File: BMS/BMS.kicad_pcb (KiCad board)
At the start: 2 copper layers, 69.4 x 66 mm, 85 parts, among them J1 Cell Taps, J10 IsoSPI, J2 IsoSPI, J3 Temp Sensors, Q1 NSV1C201MZ4, Q2 BSS308PE, Q3 BSS308PE, Q4 BSS308PE, Q5 BSS308PE, Q6 BSS308PE, Q7 BSS308PE, Q8 BSS308PE, SW1 SW_DIP_x04, U1 LTC6811, U2 ADG708

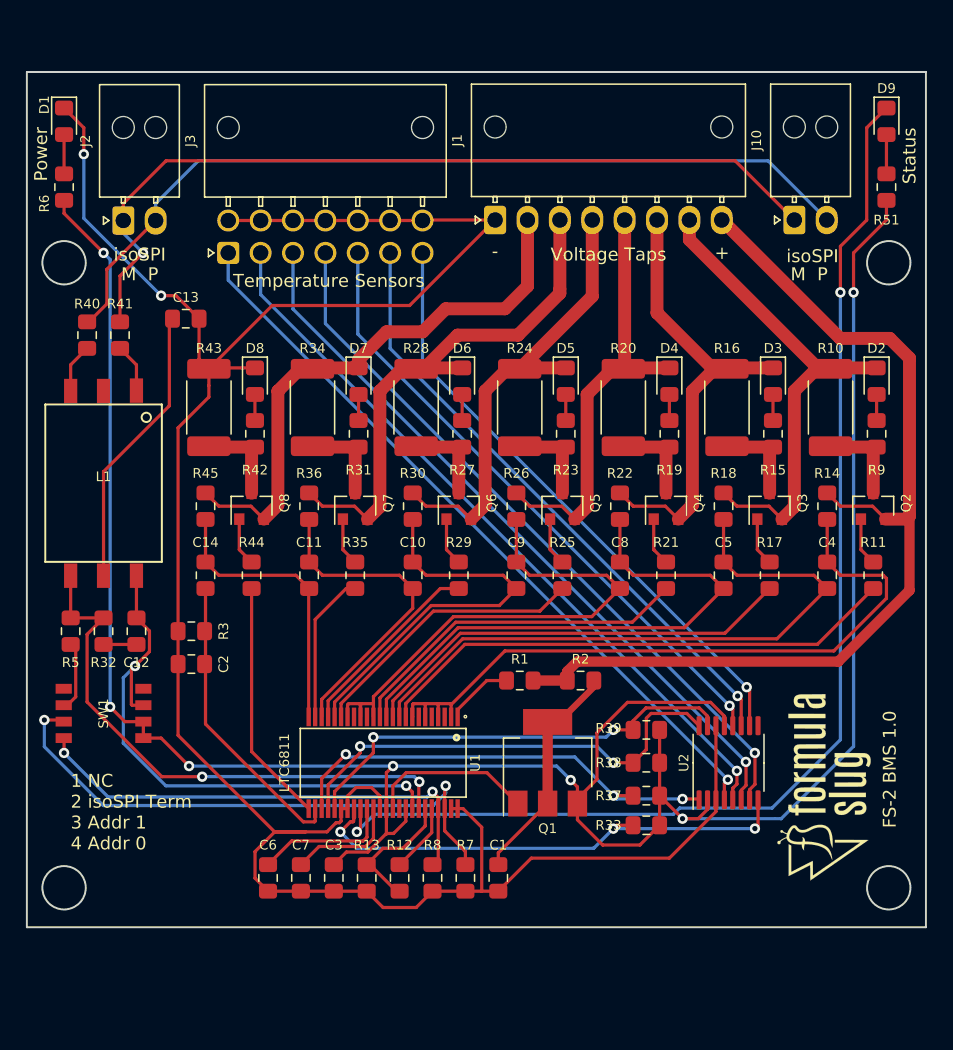
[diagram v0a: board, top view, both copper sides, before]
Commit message: Add PTC fusing to BMS board and finish layout v1.0
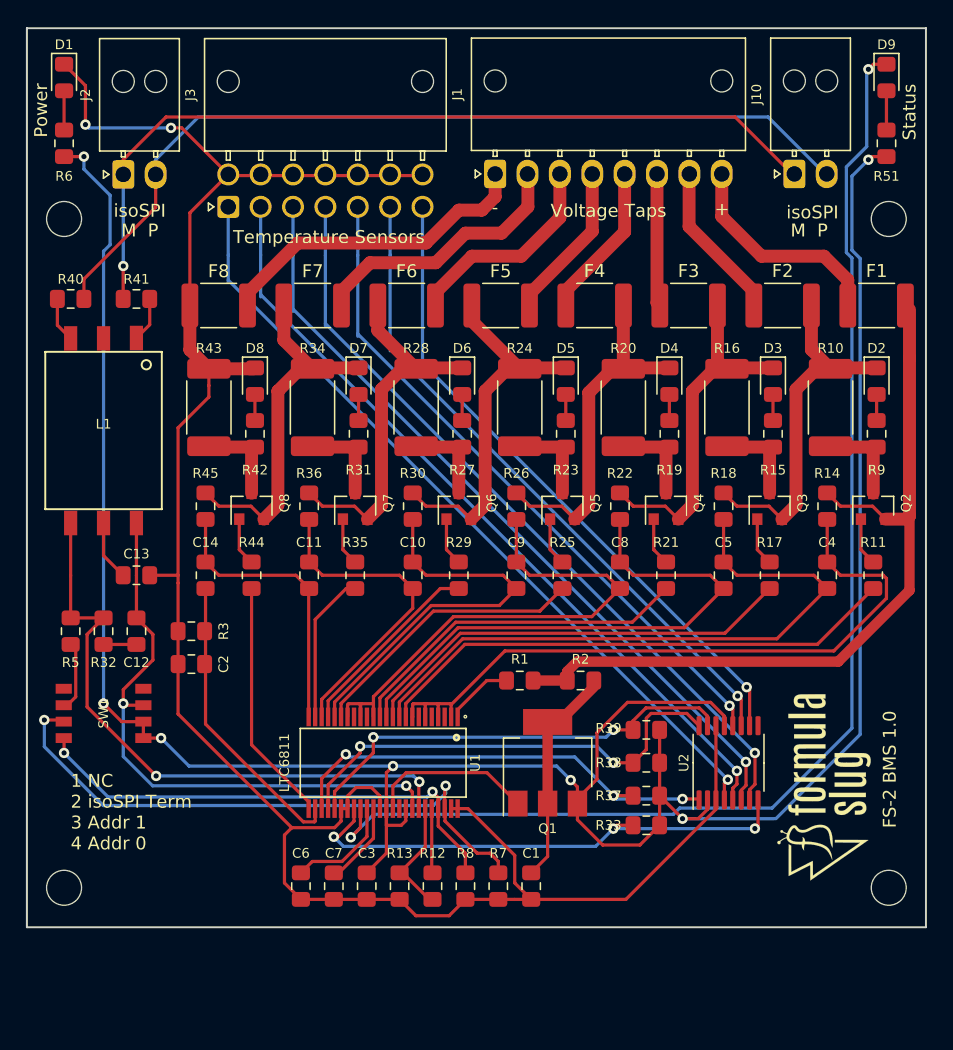
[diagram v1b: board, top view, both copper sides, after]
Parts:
- added ?: MountingHole_2.7mm_M2.5, MountingHole:MountingHole_2.7mm_M2.5, F.Cu at (90.9, 69.8)
- added ?: MountingHole_2.7mm_M2.5, MountingHole:MountingHole_2.7mm_M2.5, F.Cu at (90.9, 121.4)
- added ?: MountingHole_2.7mm_M2.5, MountingHole:MountingHole_2.7mm_M2.5, F.Cu at (154.6, 121.4)
- added ?: MountingHole_2.7mm_M2.5, MountingHole:MountingHole_2.7mm_M2.5, F.Cu at (154.7, 69.8)
- added F1: Polyfuse, Fuse:Fuse_1812_4532Metric_Pad1.30x3.40mm_HandSolder, F.Cu at (153.7, 76.5)
- added F2: Polyfuse, Fuse:Fuse_1812_4532Metric_Pad1.30x3.40mm_HandSolder, F.Cu at (146.4, 76.5)
- added F3: Polyfuse, Fuse:Fuse_1812_4532Metric_Pad1.30x3.40mm_HandSolder, F.Cu at (139.2, 76.5)
- added F4: Polyfuse, Fuse:Fuse_1812_4532Metric_Pad1.30x3.40mm_HandSolder, F.Cu at (131.9, 76.5)
- added F5: Polyfuse, Fuse:Fuse_1812_4532Metric_Pad1.30x3.40mm_HandSolder, F.Cu at (124.6, 76.5)
- added F6: Polyfuse, Fuse:Fuse_1812_4532Metric_Pad1.30x3.40mm_HandSolder, F.Cu at (117.4, 76.5)
- added F7: Polyfuse, Fuse:Fuse_1812_4532Metric_Pad1.30x3.40mm_HandSolder, F.Cu at (110.1, 76.5)
- added F8: Polyfuse, Fuse:Fuse_1812_4532Metric_Pad1.30x3.40mm_HandSolder, F.Cu at (102.9, 76.5)
- D1: value LTST-S220KGKT -> LH R974-LP-1
- moved C13 20.2 mm to (96.5, 97.3)
- moved L1 4.06 mm to (94.0, 86.1)
- moved J1 3.56 mm to (124.2, 66.3)
- moved J10 3.56 mm to (147.3, 66.3)
- moved J2 3.56 mm to (95.5, 66.3)
- moved J3 3.56 mm to (103.6, 68.8)
- moved R51 3.38 mm to (154.4, 63.9)
- moved R6 3.38 mm to (90.9, 63.9)
- moved D1 3.38 mm to (90.9, 58.9)
- moved D9 3.38 mm to (154.4, 58.9)
- moved R40 3.07 mm to (91.4, 75.9), turned to 180 degrees
- moved R41 3.07 mm to (96.5, 75.9), turned to 0 degrees
- moved C1 2.62 mm to (127.0, 121.3)
- moved C7 2.62 mm to (111.8, 121.3)
- moved R13 2.62 mm to (116.8, 121.3)
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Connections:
- J1 pad 1: V- -> Net-(F8-Pad2)
- J1 pad 2: /BB1/B# -> Net-(F7-Pad2)
- J1 pad 3: /BB2/B# -> Net-(F6-Pad2)
- J1 pad 4: /BB3/B# -> Net-(F5-Pad2)
- J1 pad 5: /BB4/B# -> Net-(F4-Pad2)
- J1 pad 6: /BB5/B# -> Net-(F3-Pad2)
- J1 pad 7: /BB6/B# -> Net-(F2-Pad2)
- J1 pad 8: /BB6/B#+1 -> Net-(F1-Pad2)
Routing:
- net Net-(F8-Pad2): track 0.00 -> 24.9 mm
- net V-: track 189.7 -> 166.9 mm
- net Net-(F7-Pad2): track 0.00 -> 21.0 mm
- net Net-(C13-Pad1): track 22.1 -> 4.66 mm
- net Net-(F1-Pad2): track 0.00 -> 17.0 mm
- net Net-(F6-Pad2): track 0.00 -> 16.4 mm
- net /BB1/B#: track 44.7 -> 29.4 mm
- net /BB6/B#+1: track 76.0 -> 61.3 mm
- net /BB2/B#: track 43.5 -> 30.4 mm
- net Net-(F2-Pad2): track 0.00 -> 12.2 mm
- net Net-(F5-Pad2): track 0.00 -> 12.2 mm
- net Net-(F4-Pad2): track 0.00 -> 12.0 mm
- net Net-(F3-Pad2): track 0.00 -> 10.2 mm
- net /BB6/B#: track 41.1 -> 30.9 mm
- net VREG: track 194.2 -> 202.9 mm
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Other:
- board size 69.4 x 66 mm -> 69.4 x 69.4 mm

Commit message: Layout v1.1 of BMS
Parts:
- removed the ? at (90.9, 69.8)
- removed the ? at (90.9, 121.4)
- removed the ? at (154.6, 121.4)
- removed the ? at (154.7, 69.8)
- removed the J3 at (103.6, 68.8)
- added ?: MountingHole_3.2mm_M3, MountingHole:MountingHole_3.2mm_M3, F.Cu at (101.9, 114.9)
- added ?: MountingHole_3.2mm_M3, MountingHole:MountingHole_3.2mm_M3, F.Cu at (101.9, 58.8)
- added ?: MountingHole_3.2mm_M3, MountingHole:MountingHole_3.2mm_M3, F.Cu at (153.7, 58.8)
- added ?: MountingHole_3.2mm_M3, MountingHole:MountingHole_3.2mm_M3, F.Cu at (153.7, 114.9)
- added J2: Temp Sensors, Connector_Molex:Molex_Nano-Fit_105314-xx14_2x07_P2.50mm_Horizontal, F.Cu at (108.8, 68.8)
- moved D9 78.0 mm to (118.0, 127.8)
- moved D1 76.8 mm to (124.8, 127.8)
- moved R51 72.4 mm to (120.3, 127.8), turned to 90 degrees
- moved R6 71.2 mm to (122.6, 127.8), turned to 90 degrees
- moved R40 70.6 mm to (145.9, 120.8), turned to 90 degrees
- moved R41 70.0 mm to (145.9, 125.5), turned to 270 degrees
- moved L1 56.1 mm to (136.1, 123.1), turned to 90 degrees
- moved J3 54.6 mm to (103.4, 120.4), turned to 270 degrees
- moved J4 54.6 mm to (154.7, 120.4), turned to 270 degrees
- moved R32 52.0 mm to (138.0, 129.3), turned to 180 degrees
- moved C12 46.4 mm to (133.7, 129.3), turned to 0 degrees
- moved C13 45.9 mm to (129.4, 129.3), turned to 180 degrees
- moved R5 38.1 mm to (123.3, 122.4), turned to 180 degrees
- moved R33 35.6 mm to (100.8, 110.1), turned to 180 degrees
- moved R37 35.6 mm to (100.8, 107.8), turned to 180 degrees
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- renumbered J2 to J3, J10 to J4
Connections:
- net /IsoSPI_N renamed /extIsoSPI_N
- net /IsoSPI_P renamed /extIsoSPI_P
- C12 pad 1: IMA -> IsoSPI_N
- L1 pad 4: IPA -> IsoSPI_P
- L1 pad 6: IMA -> IsoSPI_N
- R32 pad 1: IPA -> IsoSPI_P
- R5 pad 1: Net-(R5-Pad1) -> IsoSPI_N
- R5 pad 2: IPA -> Net-(R5-Pad2)
- SW1 pad 2: Net-(R5-Pad1) -> IsoSPI_P
- SW1 pad 7: IMA -> Net-(R5-Pad2)
- U1 pad 41: IMA -> IsoSPI_N
- U1 pad 42: IPA -> IsoSPI_P
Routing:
- net VREG: track 202.9 -> 88.3 mm, vias 7 -> 2
- net Net-(D9-Pad1): track 98.0 -> 34.0 mm, vias 2 -> 0
- net IPA: track 47.4 -> 0.00 mm, vias 2 -> 0
- net IMA: track 45.8 -> 0.00 mm, vias 2 -> 0
- net IsoSPI_P: track 0.00 -> 32.4 mm, vias 0 -> 2
- net A1: track 46.5 -> 21.0 mm
- net IsoSPI_N: track 0.00 -> 23.6 mm
- net TEMP: track 40.4 -> 18.7 mm
- net A0: track 39.1 -> 18.5 mm
- net Net-(J2-Pad1): track 62.1 -> 44.0 mm
- net MUX_A0: track 35.2 -> 18.1 mm, vias 3 -> 2
- net Net-(J2-Pad2): track 61.3 -> 44.9 mm
- net Net-(J2-Pad3): track 60.6 -> 45.7 mm
- net Net-(J2-Pad4): track 59.9 -> 46.6 mm
- net MUX_A1: track 35.9 -> 23.5 mm
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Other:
- board size 69.4 x 69.4 mm -> 59.4 x 76.8 mm
- board text added: "1"
- board text added: "1 Addr 0 2 Addr 1 3 isoSPI Term 4 NC"
- board text added: "7"
- board text added: "FS-2 BMS 1.1"
- board text added: "IPA IMA"
- board text added: "Temp Sense"
- board text removed: "1 NC 2 isoSPI Term 3 Addr 1 4 Addr 0"
- board text removed: "FS-2 BMS 1.0"
- board text removed: "M P"
- board text removed: "Temperature Sensors"

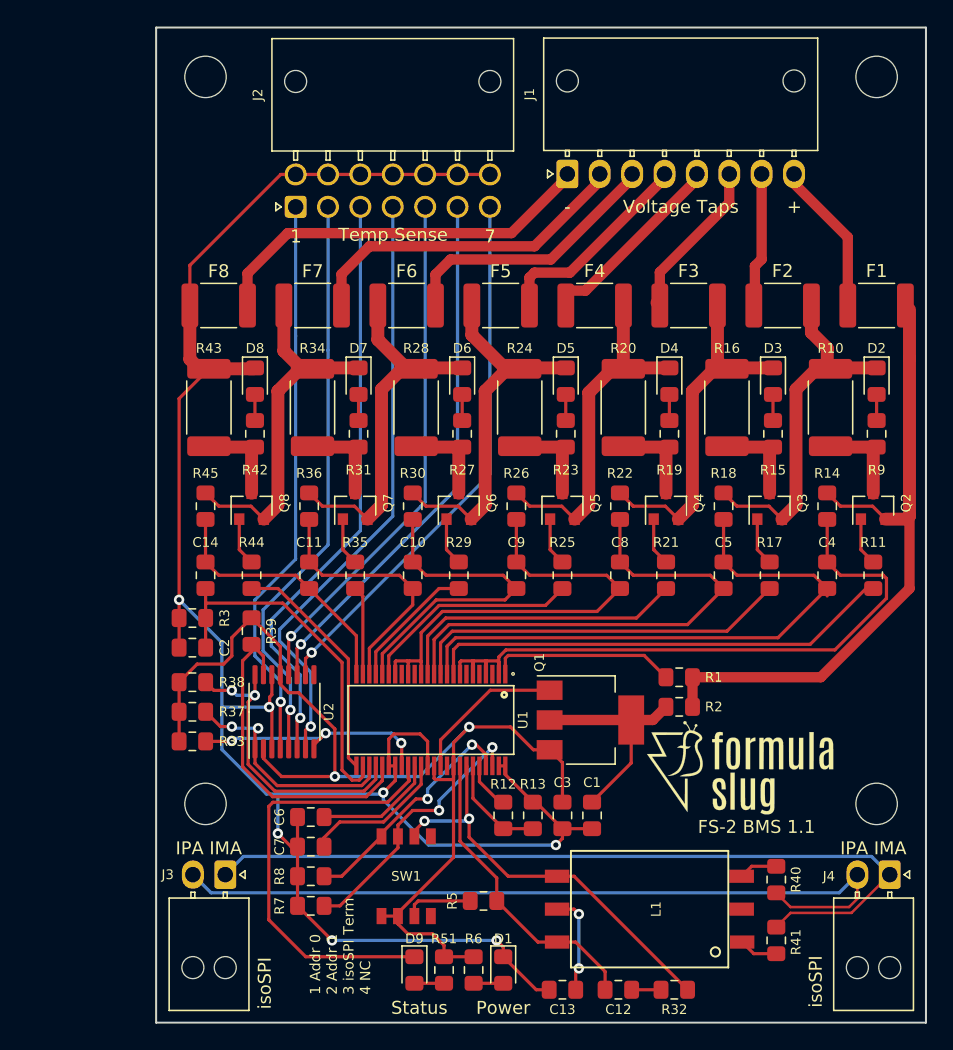
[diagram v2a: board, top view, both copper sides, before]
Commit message: Add V- plane to BMS module
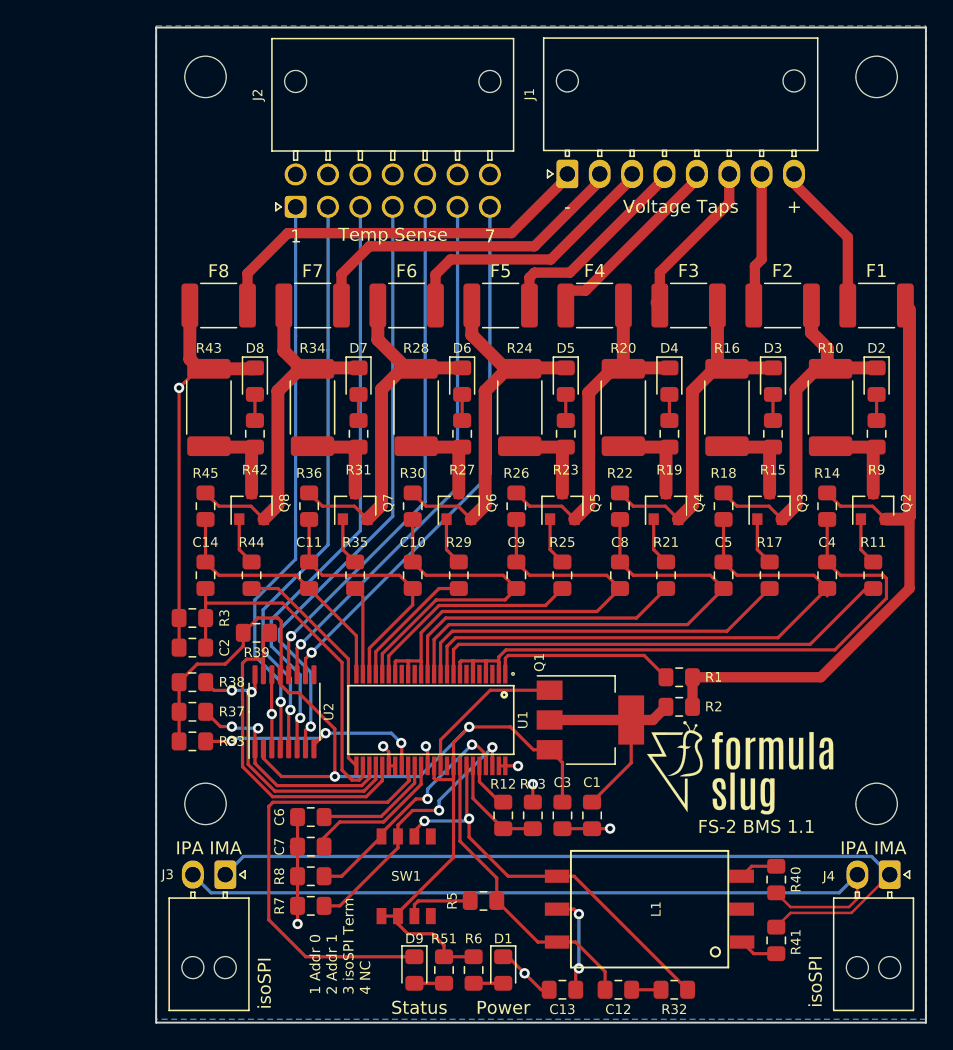
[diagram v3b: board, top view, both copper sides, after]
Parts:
- moved R39 0.40 mm to (105.8, 101.7), turned to 180 degrees
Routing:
- net V-: track 169.4 -> 62.6 mm, vias 7 -> 9
- net VREG: track 88.3 -> 89.2 mm
- net MUX_A2: track 25.9 -> 26.6 mm
- added copper zone on B.Cu, net V-

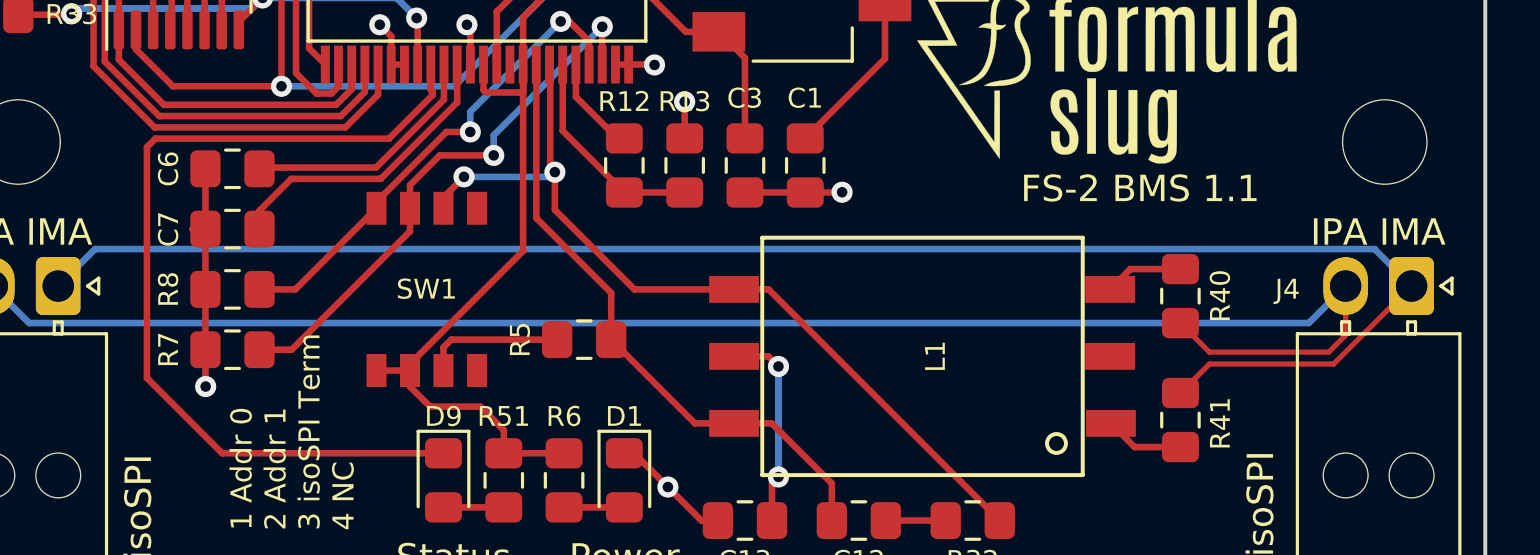
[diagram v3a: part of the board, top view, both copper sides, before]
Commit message: Add via to V- resistors on BMS
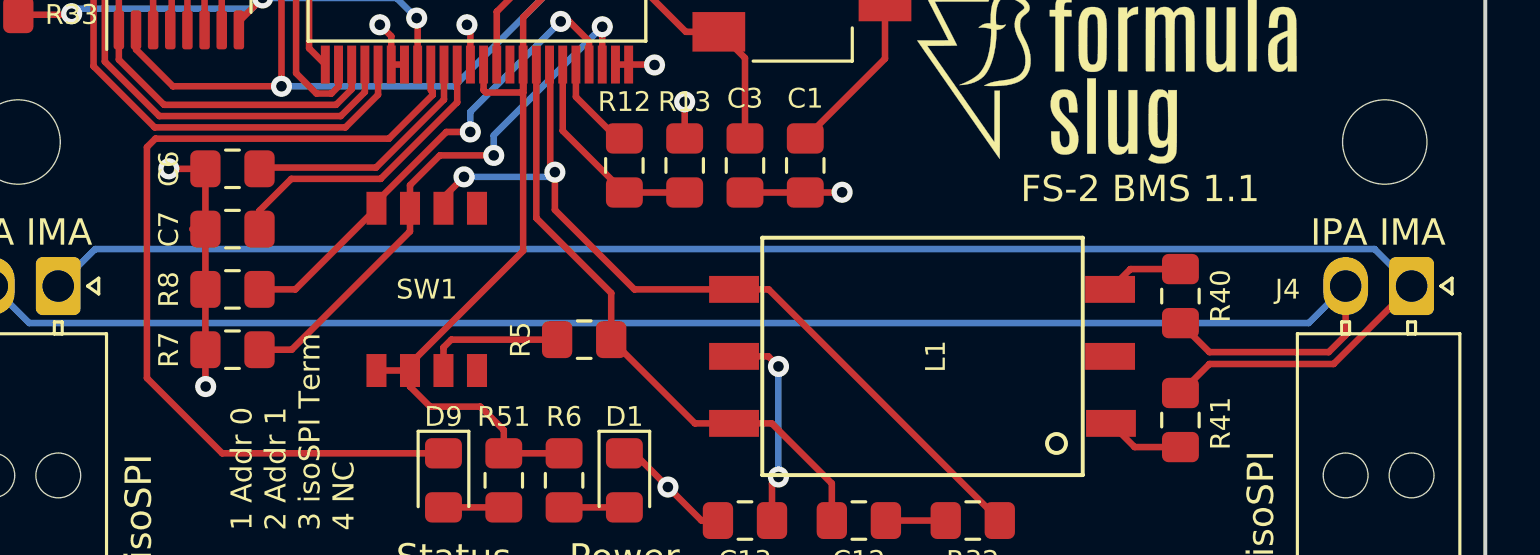
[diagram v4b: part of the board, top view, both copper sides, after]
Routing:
- net V-: track 62.6 -> 64.0 mm, vias 9 -> 10

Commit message: Repair BMS Symbols
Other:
- net class Balance removed
- net class Default removed
